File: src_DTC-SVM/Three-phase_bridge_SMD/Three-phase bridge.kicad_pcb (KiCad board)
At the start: 2 copper layers, 377.2 x 318 mm, 92 parts, among them M1 MCP6022-I/P, M2 MCP6022-I/P, P1 CONN_1, P2 POWER_FUSE, P3 CONN_2, P4 CONN_1, P5 CONN_1, P6 POWER_FUSE

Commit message: PCB update.
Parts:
- P3: footprint Battery_2x1 -> pin_2
- moved P3 12.1 mm to (161.0, 79.8)
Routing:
- net VCC: track 254.2 -> 305.3 mm
- net +48V: track 385.8 -> 397.2 mm
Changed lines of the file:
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@@
   (general
     (links 262)
-    (no_connects 5)
+    (no_connects 3)
     (area -125.780001 -108.254001 251.510001 219.695888)
     (thickness 1.6)
     (drawings 7)
-    (tracks 1215)
+    (tracks 1226)
     (zones 0)
     (modules 92)
@@
   )
   (setup
-    (last_trace_width 1.905)
+    (last_trace_width 3.81)
     (user_trace_width 0.381)
     (user_trace_width 0.508)
@@
     )
   )
-  (module Battery_2x1 (layer F.Cu)
-    (at 165.1 91.186 270)
-    (descr "Double rangee de contacts 2 x 5 pins")
-    (tags CONN)
-    (fp_text reference P3 (at -4.699 -2.54 270) (layer F.SilkS)
-      (effects (font (size 1.016 1.016) (thickness 0.2032)))
-    )
-    (fp_text value CONN_2 (at -5.08 2.921 270) (layer F.SilkS) hide
-      (effects (font (size 1.016 1.016) (thickness 0.2032)))
-    )
-    (fp_line (start -10.795 -1.27) (end -10.795 1.27) (layer F.SilkS) (width 0.254))
-    (fp_line (start -0.635 -1.27) (end -10.795 -1.27) (layer F.SilkS) (width 0.254))
-    (fp_line (start -0.635 1.27) (end -10.795 1.27) (layer F.SilkS) (width 0.254))
-    (fp_line (start 9.398 1.27) (end -0.762 1.27) (layer F.SilkS) (width 0.254))
-    (fp_line (start 9.398 -1.27) (end -0.762 -1.27) (layer F.SilkS) (width 0.254))
-    (fp_line (start 9.398 1.27) (end 9.398 -1.27) (layer F.SilkS) (width 0.254))
-    (pad 1 thru_hole rect (at -9.525 0 270) (size 1.905 1.905) (drill 0.127)
-      (layers *.Cu *.Mask F.SilkS)
-      (net 2 +48V)
-    )
-    (pad 2 thru_hole circle (at 8.128 0 270) (size 1.905 1.905) (drill 0.127)
-      (layers *.Cu *.Mask F.SilkS)
-      (net 93 VCC)
-    )
-    (model pin_array\pins_array_4x1.wrl
-      (at (xyz 0 0 0))
-      (scale (xyz 1 1 1))
-      (rotate (xyz 0 0 0))
-    )
-  )
   (module TO220_Big_Heat_Sink_Drain_Sink (layer B.Cu)
     (at 215.265 93.726)
@@
     )
   )
+  (module pin_2 (layer F.Cu)
+    (at 161.036 79.756 270)
+    (descr "Connecteurs 2 pins")
+    (tags "CONN DEV")
+    (fp_text reference P3 (at 0 2.54 270) (layer F.SilkS)
+      (effects (font (size 0.762 0.762) (thickness 0.1524)))
+    )
+    (fp_text value CONN_2 (at 0 -1.905 270) (layer F.SilkS) hide
+      (effects (font (size 0.762 0.762) (thickness 0.1524)))
+    )
+    (fp_line (start -2.54 1.27) (end -2.54 -1.27) (layer F.SilkS) (width 0.1524))
+    (fp_line (start -2.54 -1.27) (end 2.54 -1.27) (layer F.SilkS) (width 0.1524))
+    (fp_line (start 2.54 -1.27) (end 2.54 1.27) (layer F.SilkS) (width 0.1524))
+    (fp_line (start 2.54 1.27) (end -2.54 1.27) (layer F.SilkS) (width 0.1524))
+    (pad 1 thru_hole rect (at -1.27 0 270) (size 1.524 1.524) (drill 1.016)
+      (layers *.Cu *.Mask F.SilkS)
+      (net 2 +48V)
+    )
+    (pad 2 thru_hole circle (at 1.27 0 270) (size 1.524 1.524) (drill 1.016)
+      (layers *.Cu *.Mask F.SilkS)
+      (net 93 VCC)
+    )
+    (model pin_array/pins_array_2x1.wrl
+      (at (xyz 0 0 0))
+      (scale (xyz 1 1 1))
+      (rotate (xyz 0 0 0))
+    )
+  )
   (gr_line (start 147.066 209.804) (end 146.05 209.804) (angle 90) (layer Edge.Cuts) (width 0.1))
   (gr_line (start 251.46 64.516) (end 251.46 209.804) (angle 90) (layer Edge.Cuts) (width 0.1))
@@
   (segment (start 168.1988 125.5014) (end 163.2458 125.5014) (width 1.905) (layer F.Cu) (net 1))
   (segment (start 163.2458 125.5014) (end 162.7124 126.0348) (width 1.905) (layer F.Cu) (net 1))
+  (segment (start 152.4762 71.7296) (end 154.2796 71.7296) (width 1.905) (layer F.Cu) (net 2) (status C00000))
+  (segment (start 154.2796 71.7296) (end 161.036 78.486) (width 1.905) (layer F.Cu) (net 2) (status C00000))
   (segment (start 245.5672 124.2568) (end 239.0394 117.729) (width 1.905) (layer B.Cu) (net 2))
   (segment (start 239.0394 117.729) (end 228.1428 117.729) (width 1.905) (layer B.Cu) (net 2))
@@
   (segment (start 188.9506 138.2522) (end 184.3786 138.2522) (width 1.905) (layer F.Cu) (net 91))
   (segment (start 188.8236 181.5592) (end 184.1246 181.5592) (width 1.905) (layer F.Cu) (net 92))
+  (segment (start 163.449 113.157) (end 161.163 113.157) (width 3.81) (layer F.Cu) (net 93))
+  (segment (start 154.178 103.759) (end 152.146 101.727) (width 3.81) (layer F.Cu) (net 93) (status C00000))
+  (segment (start 154.178 106.172) (end 154.178 103.759) (width 3.81) (layer F.Cu) (net 93) (status 800000))
+  (segment (start 161.163 113.157) (end 154.178 106.172) (width 3.81) (layer F.Cu) (net 93))
+  (segment (start 163.6776 113.157) (end 163.449 113.157) (width 3.81) (layer F.Cu) (net 93))
+  (segment (start 161.036 81.026) (end 161.036 96.012) (width 1.905) (layer F.Cu) (net 93) (status 400000))
+  (segment (start 163.6776 98.6536) (end 163.6776 113.157) (width 1.905) (layer F.Cu) (net 93))
+  (segment (start 163.6776 113.157) (end 163.6776 113.2586) (width 1.905) (layer F.Cu) (net 93))
+  (segment (start 161.036 96.012) (end 163.6776 98.6536) (width 1.905) (layer F.Cu) (net 93))
   (segment (start 198.8312 178.7652) (end 198.3486 178.2826) (width 1.905) (layer B.Cu) (net 93))
   (segment (start 198.3486 168.6814) (end 199.7964 167.2336) (width 1.905) (layer B.Cu) (net 93))
@@
   (segment (start 152.146 101.727) (end 163.6776 113.2586) (width 1.905) (layer F.Cu) (net 93))
   (segment (start 163.6776 113.2586) (end 163.6776 113.3856) (width 1.905) (layer F.Cu) (net 93))
-  (via (at 163.6776 113.3856) (size 0.254) (layers F.Cu B.Cu) (net 93))
-  (segment (start 163.6776 113.3856) (end 163.6776 115.9002) (width 1.905) (layer B.Cu) (net 93))
   (segment (start 163.6776 115.9002) (end 168.1988 120.4214) (width 1.905) (layer B.Cu) (net 93))
+  (segment (start 163.6776 113.3856) (end 163.6776 115.9002) (width 7.62) (layer B.Cu) (net 93))
+  (via (at 163.6776 113.3856) (size 0.254) (layers F.Cu B.Cu) (net 93))
   (segment (start 186.2963 199.0217) (end 186.8678 199.5932) (width 1.27) (layer F.Cu) (net 93))
   (segment (start 186.8678 199.5932) (end 186.8678 202.438) (width 1.27) (layer F.Cu) (net 93))

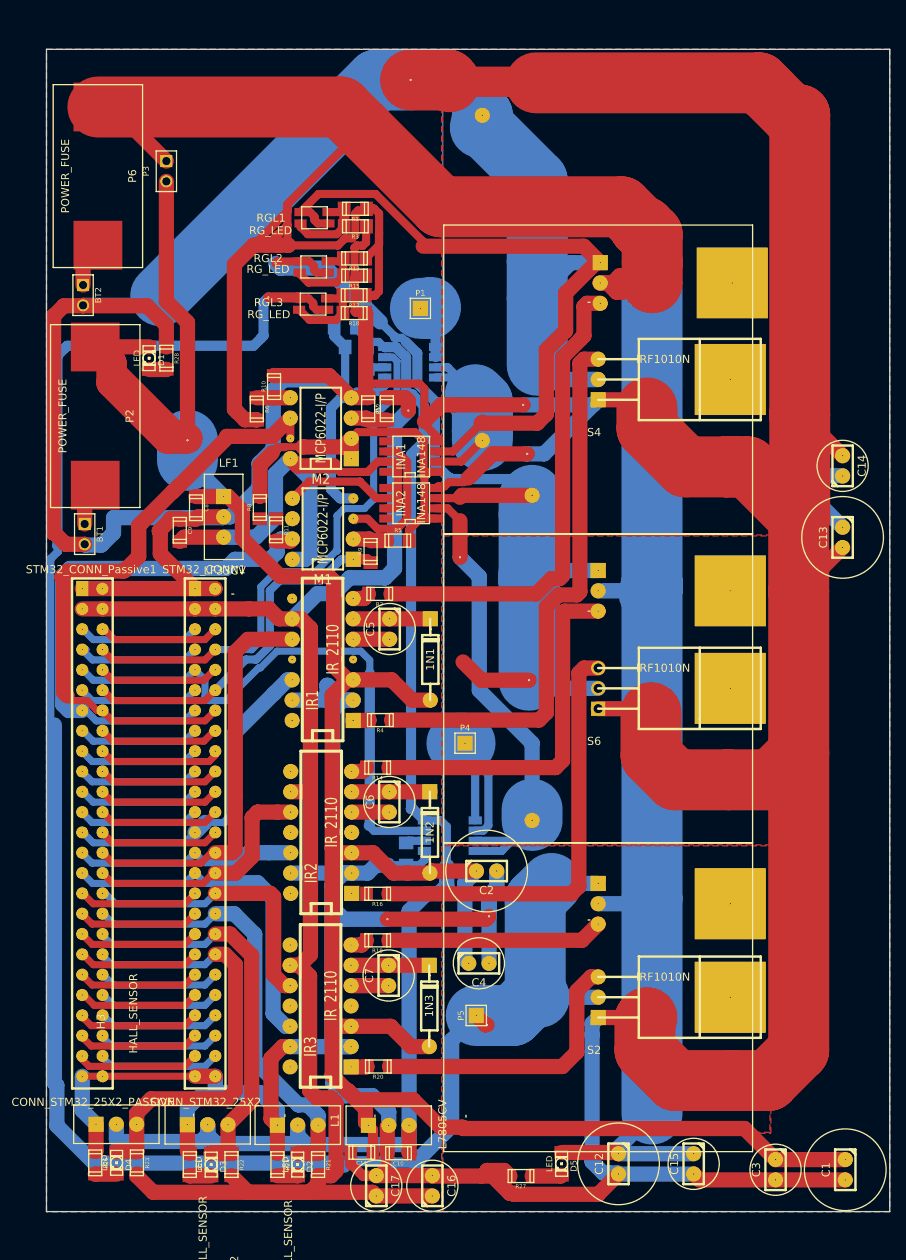
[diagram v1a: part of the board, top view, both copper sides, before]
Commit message: PCB holes and fillzones fixed on the Three-phase_bridge_SMD design.
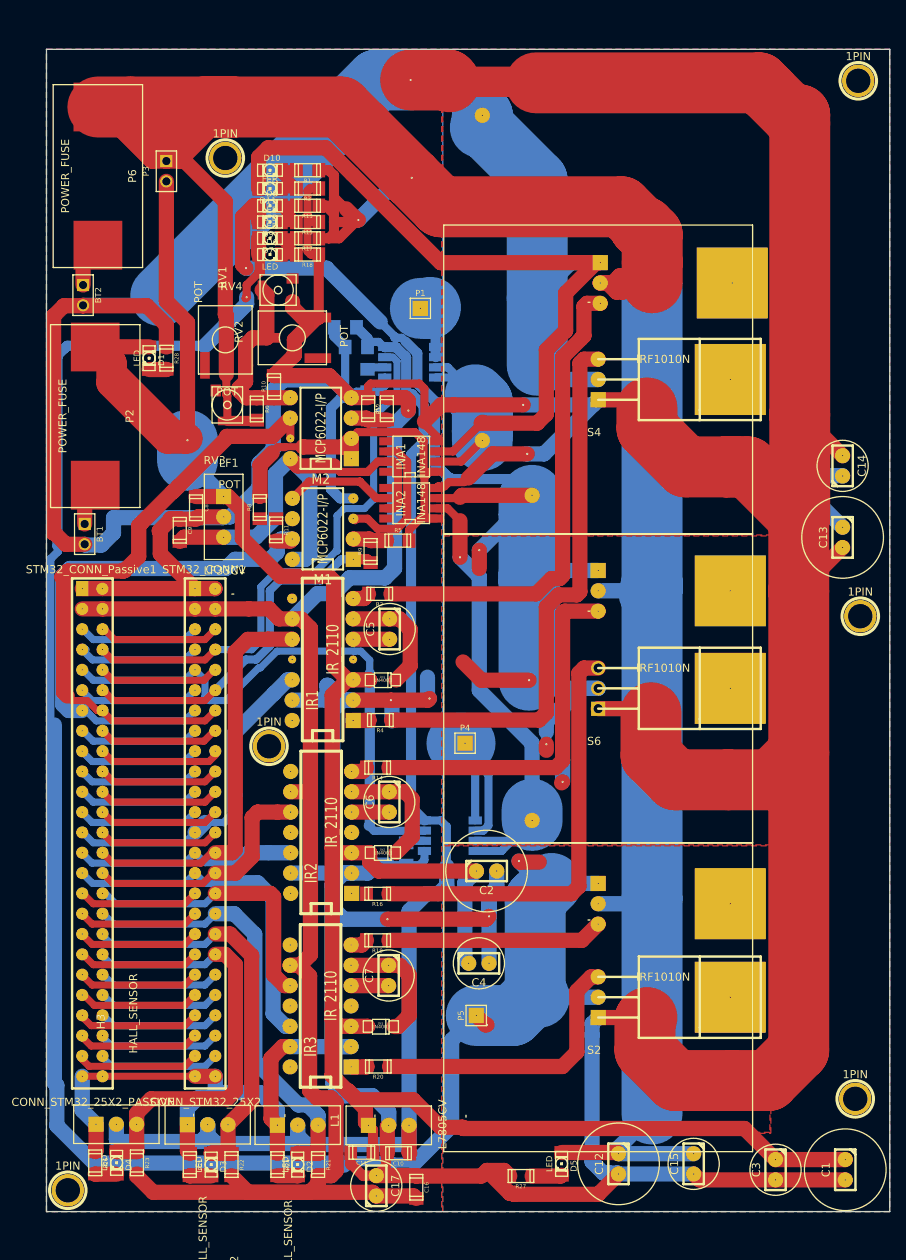
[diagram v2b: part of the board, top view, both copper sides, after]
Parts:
- removed RGL1, RGL2, RGL3: RG_LED, LED_RG_1206
- added 1PIN: P***, 1pin, F.Cu at (247.5, 68.5)
- added 1PIN: P***, 1pin, F.Cu at (247.1, 195.7)
- added 1PIN: P***, 1pin, F.Cu at (247.8, 135.4)
- added 1PIN: P***, 1pin, F.Cu at (148.7, 207.1)
- added 1PIN: P***, 1pin, F.Cu at (173.9, 151.6)
- added 1PIN: P***, 1pin, F.Cu at (168.4, 78.1)
- added D10: LED, LED-1206, F.Cu at (174.0, 79.6)
- added D11: LED, LED-1206, F.Cu at (174.0, 81.9)
- added D6: LED, LED-1206, F.Cu at (174.0, 90.2)
- added D7: LED, LED-1206, F.Cu at (174.0, 88.1)
- added D8: LED, LED-1206, F.Cu at (174.0, 84.1)
- added D9: LED, LED-1206, F.Cu at (174.0, 86.1)
- added RV1: POT, Trimmer_20K_1.5mmW_4.5mmL_3.8mmH, F.Cu at (175.0, 94.6)
- added RV2: POT, Trimmer_100K_5.21mmW_6.71mmL, F.Cu at (176.8, 100.6)
- added RV3: POT, Trimmer_20K_1.5mmW_4.5mmL_3.8mmH, F.Cu at (168.7, 109.0)
- added RV4: POT, Trimmer_100K_5.21mmW_6.71mmL, F.Cu at (168.4, 100.8)
- 1N1, 1N2, 1N3: footprint DO-41 -> SOD-123
- C16: footprint 6mm_C -> c_1206
- moved R18 9.35 mm to (178.7, 90.2)
- moved R17 9.19 mm to (178.7, 88.1)
- moved R15 8.91 mm to (178.7, 86.1)
- moved R13 8.82 mm to (178.7, 84.1)
- moved R1 7.68 mm to (178.7, 79.6)
- moved R3 7.61 mm to (178.7, 81.9)
- moved 1N3 6.60 mm to (187.8, 186.7), turned to 0 degrees
- moved 1N1 6.48 mm to (188.1, 143.4), turned to 0 degrees
- moved 1N2 6.43 mm to (188.1, 165.0), turned to 0 degrees
- moved C16 2.01 mm to (192.3, 206.8), turned to 270 degrees
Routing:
- net +48V: track 397.2 -> 459.1 mm, vias 0 -> 2
- net N-0000045: track 128.5 -> 170.2 mm, vias 2 -> 5
- net GND: track 912.8 -> 932.9 mm, vias 6 -> 8
- net N-0000038: track 4.19 -> 22.1 mm
- net VCC: track 305.3 -> 288.4 mm
- net N-0000015: track 146.1 -> 152.5 mm
- net N-000004: track 9.78 -> 15.5 mm
- net N-000008: track 9.78 -> 15.3 mm
- net N-0000017: track 9.65 -> 14.7 mm
- net N-0000044: track 11.1 -> 6.83 mm
- net N-0000040: track 10.8 -> 6.58 mm
- net N-0000041: track 10.7 -> 6.58 mm
- net N-0000055: track 246.8 -> 250.7 mm, vias 2 -> 3
- net VDD: track 199.8 -> 197.9 mm

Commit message: -Trimmers for sensing 12V and 48V have been added to the PCB design. -A visual recheck has been performed to assure that the PCB connection are connected correctly.  It seems that it is ready for the first trial with a laser cutting machine.
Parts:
- moved C4 3.90 mm to (196.2, 179.1)
- moved 1PIN 0.28 mm to (168.1, 78.2)
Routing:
- net N-0000019: track 77.4 -> 88.0 mm
- net N-0000011: track 0.00 -> 4.06 mm
- net N-0000044: track 6.83 -> 9.90 mm
- net N-000002: track 0.00 -> 1.88 mm
- net VCC: track 288.4 -> 289.9 mm
- net GND: track 932.9 -> 932.1 mm
